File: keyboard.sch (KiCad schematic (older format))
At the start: 24 parts, among them J1 USB_MINI-B, P1 ISP, P2 GPIO_CLUSTER1, P3 GPIO_CLUSTER2, U1 ATMEGA32U4, X1 CRYSTAL

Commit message: Chicory init commit from Daisy
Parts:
- removed C10, C9: 100nF, capacitors:C_0805, symbol C
- removed P2: GPIO_CLUSTER1, connectors:Socket_Strip_Straight_2x04_Pitch2.54mm, symbol CONN_02X04
- added D43: D_Schottky_Small_ALT, diodes:D_0805_V2, symbol D_Schottky_Small_ALT
- added D44: LED, diodes:D_0805_V2, symbol LED
- added J2: Conn_01x02, Connectors_JST:JST_GH_SM02B-GHS-TB_02x1.25mm_Angled, symbol Conn_01x02
- added R3, R8: 100K, resistors:R_0805_V1, symbol R
- added R9: 1K, resistors:R_0805_V1, symbol R
- added U2: SPX3819M5-L-3-3, TO_SOT_Packages_SMD:SOT-23-5, symbol SPX3819M5-L-3-3
- added U4: MCP73831, TO_SOT_Packages_SMD:SOT-23-5_HandSoldering, symbol MCP73831
- C5: value 1uF -> 10uf
- C6, C7, C8: value 100nF -> 10uf
- R5: footprint resistors:R_0805 -> resistors:R_0805_V1
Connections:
- net labels added: +BATT, VBUS
- wire segments 150 -> 158
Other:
- moved on the sheet: JP1, JP2, P3, R6, R7

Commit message: 2017年10月29日
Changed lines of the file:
@@
 F7 "SS" B L 8550 1350 60
 F8 "IRQ" B L 8550 1450 60
+F9 "GPIO5" B L 8550 1550 60
 $EndSheet
 Entry Wire Line
@@
 Connection ~ 2650 2500
 Connection ~ 3000 1200
+Entry Wire Line
+	8150 1650 8250 1550
+Wire Wire Line
+	8250 1550 8550 1550
+Text Label 8300 1550 0    60   ~ 0
+GPIO5
 $EndSCHEMATC

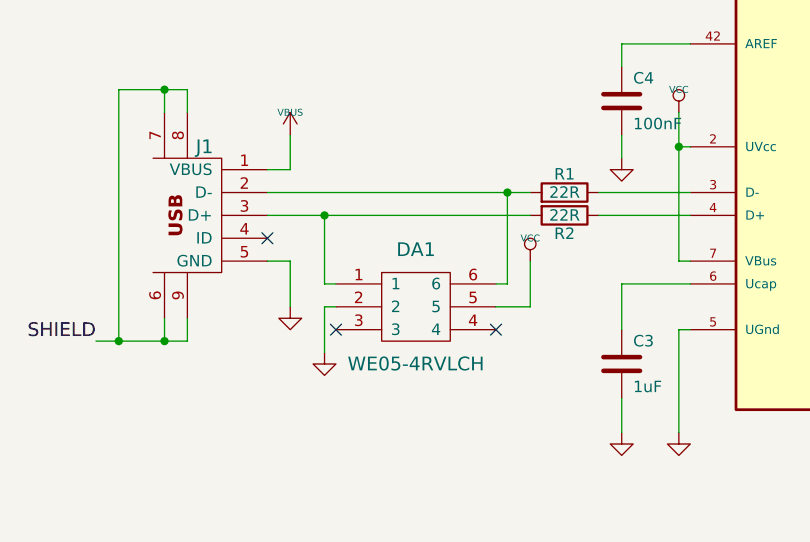
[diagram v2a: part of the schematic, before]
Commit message: complete without ble led
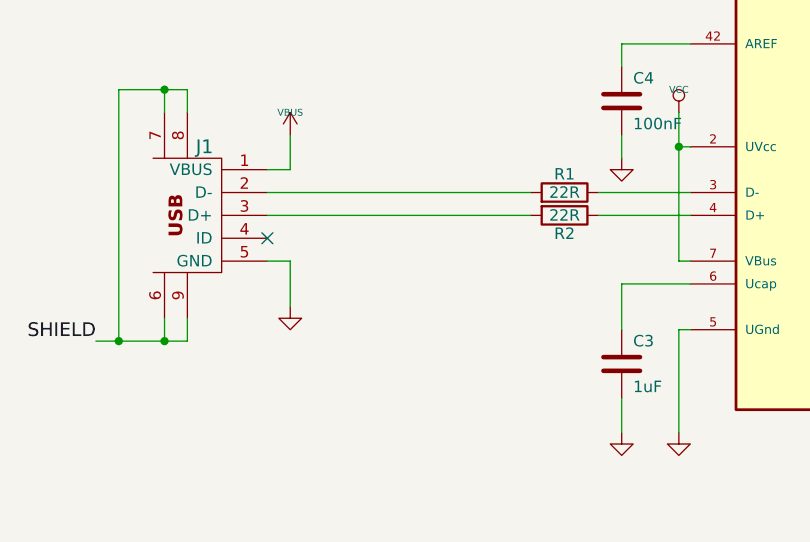
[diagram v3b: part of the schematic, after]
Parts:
- removed DA1: WE05-4RVLCH, diodes:SOT-23-6_Handsoldering, symbol WE05-4RVLCH
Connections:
- no-connect marks 3 -> 1
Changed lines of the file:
@@
 $EndComp
-$Comp
-L WE05-4RVLCH DA1
-U 1 1 592F9362
-P 2850 5700
-F 0 "DA1" H 2850 5950 60  0000 C CNN
-F 1 "WE05-4RVLCH" H 2850 5450 60  0000 C CNN
-F 2 "diodes:SOT-23-6_Handsoldering" H 2850 5700 60  0001 C CNN
-F 3 "" H 2850 5700 60  0000 C CNN
-	1    2850 5700
-	1    0    0    -1
-$EndComp
-$Comp
-L GND #PWR023
-U 1 1 592FB5F7
-P 2450 5900
-F 0 "#PWR023" H 2450 5900 30  0001 C CNN
-F 1 "GND" H 2450 5830 30  0001 C CNN
-F 2 "" H 2450 5900 60  0000 C CNN
-F 3 "" H 2450 5900 60  0000 C CNN
-	1    2450 5900
-	1    0    0    -1
-$EndComp
-$Comp
-L VCC #PWR024
-U 1 1 592FB7B1
-P 3350 5500
-F 0 "#PWR024" H 3350 5600 30  0001 C CNN
-F 1 "VCC" H 3350 5600 30  0000 C CNN
-F 2 "" H 3350 5500 60  0000 C CNN
-F 3 "" H 3350 5500 60  0000 C CNN
-	1    3350 5500
-	1    0    0    -1
-$EndComp
-NoConn ~ 3200 5800
-NoConn ~ 2500 5800
 $Comp
 L R R6
@@
 	4050 5300 3650 5300
 Wire Wire Line
-	2200 5200 3350 5200
-Wire Wire Line
-	2200 5300 3350 5300
-Wire Wire Line
-	2500 5600 2450 5600
-Wire Wire Line
-	2500 5700 2450 5700
-Wire Wire Line
-	2450 5700 2450 5900
-Wire Wire Line
-	3200 5700 3350 5700
-Wire Wire Line
-	3350 5700 3350 5500
-Wire Wire Line
-	3200 5600 3250 5600
-Wire Wire Line
-	2450 5600 2450 5300
-Connection ~ 2450 5300
-Wire Wire Line
-	3250 5600 3250 5200
-Connection ~ 3250 5200
-Wire Wire Line
 	8750 2100 8750 2050
 Wire Wire Line
@@
 Text Label 8300 1550 0    60   ~ 0
 GPIO5
+Wire Wire Line
+	3350 5200 2200 5200
+Wire Wire Line
+	2200 5300 3350 5300
 $EndSCHEMATC

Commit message: v0.1 complete
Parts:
- added SW43: DIP-TOGGLE-SWITCH(3P-9X3.5MM), switches:toggle, symbol DIP-TOGGLE-SWITCH(3P-9X3.5MM)
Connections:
- net +BATT: now also SW43.2 (COM); no longer J2.1 (Pin_1)
- new net: J2.1 (Pin_1), SW43.3 (B)
- no-connect marks 1 -> 3
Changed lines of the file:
@@
 $EndComp
 $Comp
-L GND #PWR01
+L GND #PWR24
 U 1 1 573FEF9F
 P 3500 4200
-F 0 "#PWR01" H 3500 4200 30  0001 C CNN
+F 0 "#PWR24" H 3500 4200 30  0001 C CNN
 F 1 "GND" H 3500 4130 30  0001 C CNN
 F 2 "" H 3500 4200 60  0000 C CNN
@@
 $EndComp
 $Comp
-L VCC #PWR02
+L VCC #PWR13
 U 1 1 573FFE51
 P 3700 2050
-F 0 "#PWR02" H 3700 2150 30  0001 C CNN
+F 0 "#PWR13" H 3700 2150 30  0001 C CNN
 F 1 "VCC" H 3700 2150 30  0000 C CNN
 F 2 "" H 3700 2050 60  0000 C CNN
@@
 $EndComp
 $Comp
-L VCC #PWR03
+L VCC #PWR17
 U 1 1 57400628
 P 5250 2050
-F 0 "#PWR03" H 5250 2150 30  0001 C CNN
+F 0 "#PWR17" H 5250 2150 30  0001 C CNN
 F 1 "VCC" H 5250 2150 30  0000 C CNN
 F 2 "" H 5250 2050 60  0000 C CNN
@@
 $EndComp
 $Comp
-L VCC #PWR04
+L VCC #PWR16
 U 1 1 5740064C
 P 5150 2050
-F 0 "#PWR04" H 5150 2150 30  0001 C CNN
+F 0 "#PWR16" H 5150 2150 30  0001 C CNN
 F 1 "VCC" H 5150 2150 30  0000 C CNN
 F 2 "" H 5150 2050 60  0000 C CNN
@@
 $EndComp
 $Comp
-L VCC #PWR05
+L VCC #PWR15
 U 1 1 57400669
 P 4950 2050
-F 0 "#PWR05" H 4950 2150 30  0001 C CNN
+F 0 "#PWR15" H 4950 2150 30  0001 C CNN
 F 1 "VCC" H 4950 2150 30  0000 C CNN
 F 2 "" H 4950 2050 60  0000 C CNN
@@
 $EndComp
 $Comp
-L VCC #PWR06
+L VCC #PWR14
 U 1 1 57400686
 P 4850 2050
-F 0 "#PWR06" H 4850 2150 30  0001 C CNN
+F 0 "#PWR14" H 4850 2150 30  0001 C CNN
 F 1 "VCC" H 4850 2150 30  0000 C CNN
 F 2 "" H 4850 2050 60  0000 C CNN
@@
 $EndComp
 $Comp
-L VBUS #PWR07
+L VBUS #PWR26
 U 1 1 574019E0
 P 2300 4950
-F 0 "#PWR07" H 2300 5050 30  0001 C CNN
+F 0 "#PWR26" H 2300 5050 30  0001 C CNN
 F 1 "VBUS" H 2300 5050 30  0000 C CNN
 F 2 "" H 2300 4950 60  0000 C CNN
@@
 NoConn ~ 2200 5400
 $Comp
-L GND #PWR08
+L GND #PWR28
 U 1 1 57401AD9
 P 2300 5700
-F 0 "#PWR08" H 2300 5700 30  0001 C CNN
+F 0 "#PWR28" H 2300 5700 30  0001 C CNN
 F 1 "GND" H 2300 5630 30  0001 C CNN
 F 2 "" H 2300 5700 60  0000 C CNN
@@
 $EndComp
 $Comp
-L VCC #PWR09
+L VCC #PWR25
 U 1 1 57402200
 P 4000 4850
-F 0 "#PWR09" H 4000 4950 30  0001 C CNN
+F 0 "#PWR25" H 4000 4950 30  0001 C CNN
 F 1 "VCC" H 4000 4950 30  0000 C CNN
 F 2 "" H 4000 4850 60  0000 C CNN
@@
 $EndComp
 $Comp
-L GND #PWR010
+L GND #PWR30
 U 1 1 57402590
 P 4000 6250
-F 0 "#PWR010" H 4000 6250 30  0001 C CNN
+F 0 "#PWR30" H 4000 6250 30  0001 C CNN
 F 1 "GND" H 4000 6180 30  0001 C CNN
 F 2 "" H 4000 6250 60  0000 C CNN
@@
 $EndComp
 $Comp
-L GND #PWR011
+L GND #PWR29
 U 1 1 5740267C
 P 3750 6250
-F 0 "#PWR011" H 3750 6250 30  0001 C CNN
+F 0 "#PWR29" H 3750 6250 30  0001 C CNN
 F 1 "GND" H 3750 6180 30  0001 C CNN
 F 2 "" H 3750 6250 60  0000 C CNN
@@
 $EndComp
 $Comp
-L GND #PWR012
+L GND #PWR33
 U 1 1 57402D78
 P 4900 6550
-F 0 "#PWR012" H 4900 6550 30  0001 C CNN
+F 0 "#PWR33" H 4900 6550 30  0001 C CNN
 F 1 "GND" H 4900 6480 30  0001 C CNN
 F 2 "" H 4900 6550 60  0000 C CNN
@@
 $EndComp
 $Comp
-L GND #PWR013
+L GND #PWR34
 U 1 1 57402EAD
 P 5000 6550
-F 0 "#PWR013" H 5000 6550 30  0001 C CNN
+F 0 "#PWR34" H 5000 6550 30  0001 C CNN
 F 1 "GND" H 5000 6480 30  0001 C CNN
 F 2 "" H 5000 6550 60  0000 C CNN
@@
 $EndComp
 $Comp
-L GND #PWR014
+L GND #PWR35
 U 1 1 57402FDC
 P 5100 6550
-F 0 "#PWR014" H 5100 6550 30  0001 C CNN
+F 0 "#PWR35" H 5100 6550 30  0001 C CNN
 F 1 "GND" H 5100 6480 30  0001 C CNN
 F 2 "" H 5100 6550 60  0000 C CNN
@@
 $EndComp
 $Comp
-L GND #PWR015
+L GND #PWR36
 U 1 1 5740303A
 P 5200 6550
-F 0 "#PWR015" H 5200 6550 30  0001 C CNN
+F 0 "#PWR36" H 5200 6550 30  0001 C CNN
 F 1 "GND" H 5200 6480 30  0001 C CNN
 F 2 "" H 5200 6550 60  0000 C CNN
@@
 $EndComp
 $Comp
-L GND #PWR016
+L GND #PWR31
 U 1 1 57403AAC
 P 6150 6250
-F 0 "#PWR016" H 6150 6250 30  0001 C CNN
+F 0 "#PWR31" H 6150 6250 30  0001 C CNN
 F 1 "GND" H 6150 6180 30  0001 C CNN
 F 2 "" H 6150 6250 60  0000 C CNN
@@
 MISO
 $Comp
-L VCC #PWR017
+L VCC #PWR5
 U 1 1 57835D2A
 P 5700 1250
-F 0 "#PWR017" H 5700 1350 30  0001 C CNN
+F 0 "#PWR5" H 5700 1350 30  0001 C CNN
 F 1 "VCC" H 5700 1350 30  0000 C CNN
 F 2 "" H 5700 1250 60  0000 C CNN
@@
 $EndComp
 $Comp
-L GND #PWR018
+L GND #PWR7
 U 1 1 57838F38
 P 5700 1650
-F 0 "#PWR018" H 5700 1650 30  0001 C CNN
+F 0 "#PWR7" H 5700 1650 30  0001 C CNN
 F 1 "GND" H 5700 1580 30  0001 C CNN
 F 2 "" H 5700 1650 60  0000 C CNN
@@
 GPIO7
 $Comp
-L VCC #PWR019
+L VCC #PWR19
 U 1 1 59206AEC
 P 8300 2350
-F 0 "#PWR019" H 8300 2450 30  0001 C CNN
+F 0 "#PWR19" H 8300 2450 30  0001 C CNN
 F 1 "VCC" H 8300 2450 30  0000 C CNN
 F 2 "" H 8300 2350 60  0000 C CNN
@@
 $EndComp
 $Comp
-L GND #PWR020
+L GND #PWR21
 U 1 1 59206C77
 P 8300 2850
-F 0 "#PWR020" H 8300 2850 30  0001 C CNN
+F 0 "#PWR21" H 8300 2850 30  0001 C CNN
 F 1 "GND" H 8300 2780 30  0001 C CNN
 F 2 "" H 8300 2850 60  0000 C CNN
@@
 $EndComp
 $Comp
-L GND #PWR021
+L GND #PWR27
 U 1 1 591F8384
 P 3750 5050
-F 0 "#PWR021" H 3750 5050 30  0001 C CNN
+F 0 "#PWR27" H 3750 5050 30  0001 C CNN
 F 1 "GND" H 3750 4980 30  0001 C CNN
 F 2 "" H 3750 5050 60  0000 C CNN
@@
 SHIELD
 $Comp
-L GND #PWR022
+L GND #PWR32
 U 1 1 59280D3C
 P 4800 6550
-F 0 "#PWR022" H 4800 6550 30  0001 C CNN
+F 0 "#PWR32" H 4800 6550 30  0001 C CNN
 F 1 "GND" H 4800 6480 30  0001 C CNN
 F 2 "" H 4800 6550 60  0000 C CNN
@@
 $EndComp
 $Comp
-L VCC #PWR025
+L VCC #PWR12
 U 1 1 592F09BC
 P 8850 2000
-F 0 "#PWR025" H 8850 2100 30  0001 C CNN
+F 0 "#PWR12" H 8850 2100 30  0001 C CNN
 F 1 "VCC" H 8850 2100 30  0000 C CNN
 F 2 "" H 8850 2000 60  0000 C CNN
@@
 $EndComp
 $Comp
-L +BATT #PWR026
+L +BATT #PWR1
 U 1 1 59C3F6A7
-P 3000 1200
-F 0 "#PWR026" H 3000 1050 50  0001 C CNN
-F 1 "+BATT" H 3000 1340 50  0000 C CNN
-F 2 "" H 3000 1200 50  0001 C CNN
-F 3 "" H 3000 1200 50  0001 C CNN
-	1    3000 1200
-	1    0    0    -1
-$EndComp
-$Comp
-L GND #PWR027
+P 2850 800
+F 0 "#PWR1" H 2850 650 50  0001 C CNN
+F 1 "+BATT" H 2850 940 50  0000 C CNN
+F 2 "" H 2850 800 50  0001 C CNN
+F 3 "" H 2850 800 50  0001 C CNN
+	1    2850 800
+	1    0    0    -1
+$EndComp
+$Comp
+L GND #PWR6
 U 1 1 59C3F751
 P 3000 1650
-F 0 "#PWR027" H 3000 1400 50  0001 C CNN
+F 0 "#PWR6" H 3000 1400 50  0001 C CNN
 F 1 "GND" H 3000 1500 50  0000 C CNN
 F 2 "" H 3000 1650 50  0001 C CNN
@@
 $EndComp
 $Comp
-L VCC #PWR028
+L VCC #PWR3
 U 1 1 59C41538
 P 2600 1000
-F 0 "#PWR028" H 2600 850 50  0001 C CNN
+F 0 "#PWR3" H 2600 850 50  0001 C CNN
 F 1 "VCC" H 2600 1150 50  0000 C CNN
 F 2 "" H 2600 1000 50  0001 C CNN
@@
 $EndComp
 $Comp
-L GND #PWR029
+L GND #PWR10
 U 1 1 59C42612
 P 2350 1850
-F 0 "#PWR029" H 2350 1600 50  0001 C CNN
+F 0 "#PWR10" H 2350 1600 50  0001 C CNN
 F 1 "GND" H 2350 1700 50  0000 C CNN
 F 2 "" H 2350 1850 50  0001 C CNN
@@
 $EndComp
 $Comp
-L GND #PWR030
+L GND #PWR11
 U 1 1 59C426CE
 P 2600 1850
-F 0 "#PWR030" H 2600 1600 50  0001 C CNN
+F 0 "#PWR11" H 2600 1600 50  0001 C CNN
 F 1 "GND" H 2600 1700 50  0000 C CNN
 F 2 "" H 2600 1850 50  0001 C CNN
@@
 Connection ~ 8950 2650
 Wire Wire Line
-	3150 1400 3000 1400
-Wire Wire Line
-	3000 1400 3000 1200
+	3000 1000 2850 1000
+Wire Wire Line
+	2850 1000 2850 800
 Wire Wire Line
 	3150 1500 3000 1500
@@
 	1600 1650 1600 1850
 $Comp
-L GND #PWR031
+L GND #PWR9
 U 1 1 59C42F91
 P 1600 1850
-F 0 "#PWR031" H 1600 1600 50  0001 C CNN
+F 0 "#PWR9" H 1600 1600 50  0001 C CNN
 F 1 "GND" H 1600 1700 50  0000 C CNN
 F 2 "" H 1600 1850 50  0001 C CNN
@@
 	700  900  700  950
 $Comp
-L +BATT #PWR032
+L +BATT #PWR2
 U 1 1 59C43A4E
 P 700 900
-F 0 "#PWR032" H 700 750 50  0001 C CNN
+F 0 "#PWR2" H 700 750 50  0001 C CNN
 F 1 "+BATT" H 700 1040 50  0000 C CNN
 F 2 "" H 700 900 50  0001 C CNN
@@
 Connection ~ 900  1250
 $Comp
-L VBUS #PWR033
+L VBUS #PWR4
 U 1 1 59C44460
 P 900 1050
-F 0 "#PWR033" H 900 1150 30  0001 C CNN
+F 0 "#PWR4" H 900 1150 30  0001 C CNN
 F 1 "VBUS" H 900 1150 30  0000 C CNN
 F 2 "" H 900 1050 60  0000 C CNN
@@
 	900  1700 900  1850
 $Comp
-L GND #PWR034
+L GND #PWR8
 U 1 1 59C47000
 P 900 1850
-F 0 "#PWR034" H 900 1600 50  0001 C CNN
+F 0 "#PWR8" H 900 1600 50  0001 C CNN
 F 1 "GND" H 900 1700 50  0000 C CNN
 F 2 "" H 900 1850 50  0001 C CNN
@@
 $EndComp
 $Comp
-L VBUS #PWR035
+L VBUS #PWR18
 U 1 1 59C47B46
 P 500 2350
-F 0 "#PWR035" H 500 2450 30  0001 C CNN
+F 0 "#PWR18" H 500 2450 30  0001 C CNN
 F 1 "VBUS" H 500 2450 30  0000 C CNN
 F 2 "" H 500 2350 60  0000 C CNN
@@
 	2650 2500 2650 2650
 $Comp
-L +BATT #PWR036
+L +BATT #PWR20
 U 1 1 59C4999A
 P 2650 2500
-F 0 "#PWR036" H 2650 2350 50  0001 C CNN
+F 0 "#PWR20" H 2650 2350 50  0001 C CNN
 F 1 "+BATT" H 2650 2640 50  0000 C CNN
 F 2 "" H 2650 2500 50  0001 C CNN
@@
 	2650 2950 2650 3000
 $Comp
-L GND #PWR037
+L GND #PWR23
 U 1 1 59C49D63
 P 2650 3000
-F 0 "#PWR037" H 2650 2750 50  0001 C CNN
+F 0 "#PWR23" H 2650 2750 50  0001 C CNN
 F 1 "GND" H 2650 2850 50  0000 C CNN
 F 2 "" H 2650 3000 50  0001 C CNN
@@
 	2500 2700 2500 3000
 $Comp
-L GND #PWR038
+L GND #PWR22
 U 1 1 59C4A8F0
 P 2500 3000
-F 0 "#PWR038" H 2500 2750 50  0001 C CNN
+F 0 "#PWR22" H 2500 2750 50  0001 C CNN
 F 1 "GND" H 2500 2850 50  0000 C CNN
 F 2 "" H 2500 3000 50  0001 C CNN
@@
 	8250 1450 8550 1450
 Connection ~ 2650 2500
-Connection ~ 3000 1200
+Connection ~ 2850 800
 Entry Wire Line
 	8150 1650 8250 1550
@@
 Wire Wire Line
 	2200 5300 3350 5300
+Wire Wire Line
+	3000 1100 3000 1400
+Wire Wire Line
+	3000 1400 3150 1400
+NoConn ~ 3000 900
+NoConn ~ 8650 1100
+$Comp
+L DIP-TOGGLE-SWITCH(3P-9X3.5MM) SW43
+U 1 1 59FF17DE
+P 3250 1000
+F 0 "SW43" H 3150 1150 50  0000 L BNN
+F 1 "DIP-TOGGLE-SWITCH(3P-9X3.5MM)" H 3150 800 50  0000 L BNN
+F 2 "switches:toggle" H 3250 1150 50  0001 C CNN
+F 3 "" H 3250 1000 60  0000 C CNN
+F 4 "311030006" H 3250 1000 60  0001 C CNN "Desc"
+F 5 "NIL" H 3250 1000 60  0001 C CNN "MFG NO"
+F 6 "NIL" H 3250 1000 60  0001 C CNN "MFR"
+F 7 "NIL" H 3250 1000 60  0001 C CNN "Notes"
+	1    3250 1000
+	1    0    0    -1
+$EndComp
 $EndSCHEMATC
